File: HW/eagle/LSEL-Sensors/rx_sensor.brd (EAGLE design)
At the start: 22 x 20 mm, 14 parts, among them U1 Tiny45-20-SMT

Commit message: Documents
datasheets, RJ information
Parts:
- JP2: value (none) -> RJ11-2L-B; device SparkFun-Connectors:JST-4-PTH -> con-tycoelectronics:RJ11-NO_SHIELD
- moved JP2 3.75 mm to (25.8, 10.0), turned to 90 degrees
- moved R2 0.25 mm to (15.0, 10.0), flipped to the bottom, turned to 90 degrees
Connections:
- net GND: now also JP2.3; no longer JP2.2
- net SCL: now also JP2.2; no longer JP2.1
- net SDA/MOSI: now also JP2.5; no longer JP2.4
- net VCC: now also JP2.4; no longer JP2.3
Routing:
- net SCL: track 36.6 -> 32.2 mm
- net N$1: track 13.0 -> 9.80 mm
- net SDA/MOSI: track 27.5 -> 25.1 mm
- net VCC: track 11.2 -> 8.99 mm, vias 3 -> 2
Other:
- board size 22 x 20 mm -> 29 x 20 mm
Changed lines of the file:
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@@
 <board>
 <plain>
-<wire x1="0" y1="0" x2="22" y2="0" width="0" layer="20"/>
-<wire x1="22" y1="0" x2="22" y2="20" width="0" layer="20"/>
-<wire x1="22" y1="20" x2="0" y2="20" width="0" layer="20"/>
+<wire x1="0" y1="0" x2="29" y2="0" width="0" layer="20"/>
+<wire x1="29" y1="0" x2="28.75" y2="20" width="0" layer="20"/>
+<wire x1="28.75" y1="20" x2="0" y2="20" width="0" layer="20"/>
 <wire x1="0" y1="20" x2="0" y2="0" width="0" layer="20"/>
 <hole x="2.5" y="17.5" drill="2"/>
@@
 <attribute name="VALUE" x="8.5" y="6.25" size="0.4064" layer="28" font="vector" ratio="15" rot="MR180"/>
 </element>
-<element name="R2" library="SparkFun-Resistors" package="0603-RES" value="1k" x="15" y="10.25" smashed="yes" rot="R270">
-<attribute name="NAME" x="14" y="12" size="0.4064" layer="25" font="vector" ratio="15" rot="R270" align="bottom-right"/>
-<attribute name="VALUE" x="14" y="8.5" size="0.4064" layer="27" font="vector" ratio="15" rot="R270"/>
+<element name="R2" library="SparkFun-Resistors" package="0603-RES" value="1k" x="15" y="10" smashed="yes" rot="MR90">
+<attribute name="NAME" x="14" y="8.25" size="0.4064" layer="26" font="vector" ratio="15" rot="MR90" align="bottom-right"/>
+<attribute name="VALUE" x="14" y="11.75" size="0.4064" layer="28" font="vector" ratio="15" rot="MR90"/>
 </element>
 <element name="R3" library="SparkFun-Resistors" package="0603-RES" value="10k" x="12.5" y="8" smashed="yes" rot="MR270">
@@
 <attribute name="VALUE" x="1" y="7.73" size="0.4064" layer="27" rot="R90"/>
 </element>
-<element name="JP2" library="SparkFun-Connectors" package="JST-4-PTH" value="" x="22" y="10" smashed="yes" rot="R270">
-<attribute name="SKU" value="PRT-09916" x="5.49" y="-9.05" size="1.778" layer="27" rot="R270" display="off"/>
-<attribute name="NAME" x="21.48" y="16.48" size="0.6096" layer="25" font="vector" ratio="15" rot="R90"/>
-<attribute name="VALUE" x="21" y="12.27" size="0.4064" layer="27" rot="R270"/>
+<element name="JP2" library="con-tycoelectronics" package="RJ11-NO_SHIELD" value="RJ11-2L-B" x="25.75" y="10" smashed="yes" rot="R90">
+<attribute name="NAME" x="26.27" y="3.52" size="0.6096" layer="25" font="vector" ratio="15" rot="R270"/>
+<attribute name="VALUE" x="26.75" y="7.73" size="0.4064" layer="27" rot="R90"/>
+<attribute name="OC_FARNELL" value="unknown" x="25.75" y="10" size="1.778" layer="27" rot="R90" display="off"/>
+<attribute name="MF" value="TYCO ELECTRONICS" x="25.75" y="10" size="1.778" layer="27" rot="R90" display="off"/>
+<attribute name="OC_NEWARK" value="83F4463" x="25.75" y="10" size="1.778" layer="27" rot="R90" display="off"/>
+<attribute name="MPN" value="RJ11-2L-B" x="25.75" y="10" size="1.778" layer="27" rot="R90" display="off"/>
 </element>
 <element name="JP3" library="pinhead" package="2X03" value="" x="11" y="2.5" smashed="yes">
@@
 <polygon width="0.4064" layer="1" spacing="0.6096">
 <vertex x="0" y="20"/>
-<vertex x="22" y="20"/>
-<vertex x="22" y="0"/>
+<vertex x="28.5" y="20"/>
+<vertex x="28.5" y="0"/>
 <vertex x="0" y="0"/>
 </polygon>
-<contactref element="JP2" pad="3"/>
+<contactref element="JP2" pad="4"/>
 <contactref element="JP1" pad="2"/>
 <wire x1="9.5" y1="13.15" x2="7.1" y2="13.15" width="0.4064" layer="16"/>
@@
 <wire x1="12.5" y1="7.15" x2="11.85" y2="7.15" width="0.4064" layer="16"/>
 <wire x1="11.85" y1="7.15" x2="10.15" y2="8.85" width="0.4064" layer="16"/>
-<via x="19.25" y="9" extent="1-16" drill="0.3"/>
-<wire x1="19.25" y1="9" x2="17" y2="9" width="1.2" layer="16"/>
 </signal>
 <signal name="GND">
@@
 <polygon width="0.4064" layer="16" spacing="0.6096">
 <vertex x="0" y="0"/>
-<vertex x="22" y="0"/>
-<vertex x="22" y="20"/>
+<vertex x="28.5" y="0"/>
+<vertex x="28.5" y="20"/>
 <vertex x="0" y="20"/>
 </polygon>
 <contactref element="JP1" pad="3"/>
-<contactref element="JP2" pad="2"/>
+<contactref element="JP2" pad="3"/>
 <contactref element="R5" pad="1"/>
 <contactref element="TSOP4836" pad="GND"/>
 <wire x1="5" y1="11" x2="6.85" y2="11" width="0.4064" layer="1"/>
 <wire x1="6.85" y1="11" x2="7" y2="10.85" width="0.4064" layer="1"/>
-<wire x1="17" y1="11" x2="14.9" y2="11" width="0.4064" layer="1"/>
-<wire x1="14.9" y1="11" x2="15" y2="11.1" width="0.4064" layer="1"/>
 <wire x1="15" y1="4.25" x2="14.5" y2="3.75" width="0.4064" layer="1"/>
 <wire x1="14.5" y1="3.75" x2="13.56" y2="3.75" width="0.4064" layer="1"/>
@@
 <wire x1="14.6282" y1="6.6218" x2="15" y2="6.25" width="0.4064" layer="1"/>
 <wire x1="15" y1="6.25" x2="15" y2="4.25" width="0.4064" layer="1"/>
+<wire x1="15" y1="9.15" x2="16.645" y2="9.15" width="0.4064" layer="16"/>
+<wire x1="16.645" y1="9.15" x2="16.86" y2="9.365" width="0.4064" layer="16"/>
 </signal>
 <signal name="N$1">
 <contactref element="LED1" pad="C"/>
 <contactref element="R2" pad="2"/>
-<wire x1="15" y1="9.4" x2="15" y2="8.5" width="0.4064" layer="1"/>
-<via x="15" y="8.5" extent="1-16" drill="0.3"/>
+<wire x1="15" y1="10.85" x2="15" y2="12" width="0.4064" layer="16"/>
+<via x="15" y="12" extent="1-16" drill="0.3"/>
 <via x="17" y="15.5" extent="1-16" drill="0.3"/>
 <wire x1="15.623" y1="19.25" x2="15.623" y2="16.877" width="0.4064" layer="1"/>
 <wire x1="15.623" y1="16.877" x2="17" y2="15.5" width="0.4064" layer="1"/>
-<wire x1="15" y1="8.5" x2="15" y2="12.75" width="0.4064" layer="16"/>
+<wire x1="15" y1="12" x2="15" y2="12.75" width="0.4064" layer="16"/>
 <wire x1="15" y1="12.75" x2="17" y2="14.75" width="0.4064" layer="16"/>
 <wire x1="17" y1="14.75" x2="17" y2="15.5" width="0.4064" layer="16"/>
@@
 <contactref element="U1" pad="7"/>
 <contactref element="JP3" pad="3"/>
-<contactref element="JP2" pad="1"/>
+<contactref element="JP2" pad="2"/>
 <contactref element="JP1" pad="4"/>
 <via x="10.25" y="11.5" extent="1-16" drill="0.3"/>
@@
 <wire x1="11.5" y1="11.5" x2="12.75" y2="10" width="0.4064" layer="16"/>
 <via x="12.75" y="10" extent="1-16" drill="0.3"/>
-<wire x1="12.75" y1="10" x2="14" y2="12.25" width="0.4064" layer="1"/>
+<wire x1="12.75" y1="10" x2="13.75" y2="8" width="0.4064" layer="1"/>
 <wire x1="11" y1="1.23" x2="12.27" y2="2.5" width="0.4064" layer="1"/>
 <wire x1="12.27" y1="2.5" x2="15" y2="2.5" width="0.4064" layer="1"/>
-<wire x1="15" y1="2.5" x2="18.5" y2="5.5" width="0.4064" layer="1"/>
-<wire x1="18.5" y1="5.5" x2="18.5" y2="13" width="0.4064" layer="1"/>
-<wire x1="18.5" y1="13" x2="17" y2="13" width="0.4064" layer="1"/>
 <wire x1="10.365" y1="13.3528" x2="10.365" y2="11.615" width="0.4064" layer="1"/>
 <wire x1="10.365" y1="11.615" x2="10.25" y2="11.5" width="0.4064" layer="1"/>
@@
 <wire x1="9.75" y1="15" x2="7" y2="15" width="0.4064" layer="1"/>
 <wire x1="7" y1="15" x2="5" y2="13" width="0.4064" layer="1"/>
-<wire x1="14" y1="12.25" x2="16.25" y2="12.25" width="0.4064" layer="1"/>
-<wire x1="16.25" y1="12.25" x2="17" y2="13" width="0.4064" layer="1"/>
+<wire x1="13.75" y1="8" x2="18.555" y2="7.75" width="0.4064" layer="1"/>
+<wire x1="18.555" y1="7.75" x2="19.4" y2="8.095" width="0.4064" layer="1"/>
+<wire x1="15" y1="2.5" x2="19" y2="6.5" width="0.4064" layer="1"/>
+<wire x1="19" y1="6.5" x2="19" y2="7.305" width="0.4064" layer="1"/>
+<wire x1="19" y1="7.305" x2="18.555" y2="7.75" width="0.4064" layer="1"/>
 </signal>
 <signal name="RST">
@@
 <contactref element="JP3" pad="4"/>
 <contactref element="JP1" pad="1"/>
-<contactref element="JP2" pad="4"/>
+<contactref element="JP2" pad="5"/>
 <wire x1="12.905" y1="13.3528" x2="12.905" y2="11.405" width="0.4064" layer="1"/>
-<wire x1="12.905" y1="11.405" x2="11.625" y2="10.125" width="0.4064" layer="1"/>
-<wire x1="11.625" y1="10.125" x2="9.75" y2="8.25" width="0.4064" layer="1"/>
+<wire x1="12.905" y1="11.405" x2="9.75" y2="8.25" width="0.4064" layer="1"/>
 <wire x1="9.75" y1="8.25" x2="8.25" y2="8.25" width="0.4064" layer="1"/>
 <wire x1="8.25" y1="8.25" x2="7" y2="7" width="0.4064" layer="1"/>
@@
 <wire x1="7" y1="5" x2="5" y2="7" width="0.4064" layer="16"/>
 <wire x1="12.905" y1="13.3528" x2="13" y2="13.3528" width="0.4064" layer="1"/>
-<wire x1="13" y1="13.3528" x2="13" y2="11.5" width="0.4064" layer="1"/>
-<wire x1="17" y1="7" x2="15.25" y2="7" width="0.4064" layer="1"/>
-<wire x1="15.25" y1="7" x2="11.625" y2="10.125" width="0.4064" layer="1"/>
+<wire x1="13" y1="13.3528" x2="13" y2="12.75" width="0.4064" layer="1"/>
+<wire x1="13" y1="11.5" x2="13" y2="12.75" width="0.4064" layer="1"/>
+<wire x1="13" y1="12.75" x2="15.515" y2="12.75" width="0.4064" layer="1"/>
+<wire x1="15.515" y1="12.75" x2="16.86" y2="11.905" width="0.4064" layer="1"/>
 </signal>
 <signal name="N$3">

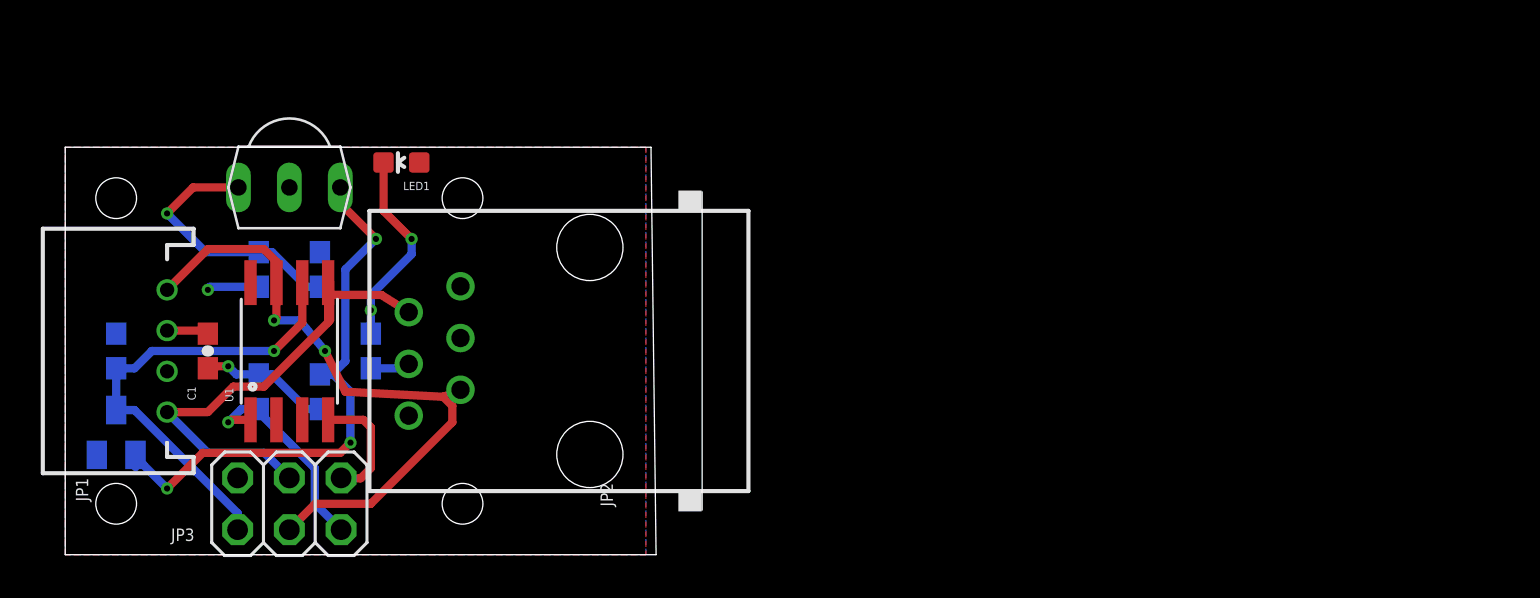
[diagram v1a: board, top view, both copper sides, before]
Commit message: Sensor RJ
Sensor connectors changed
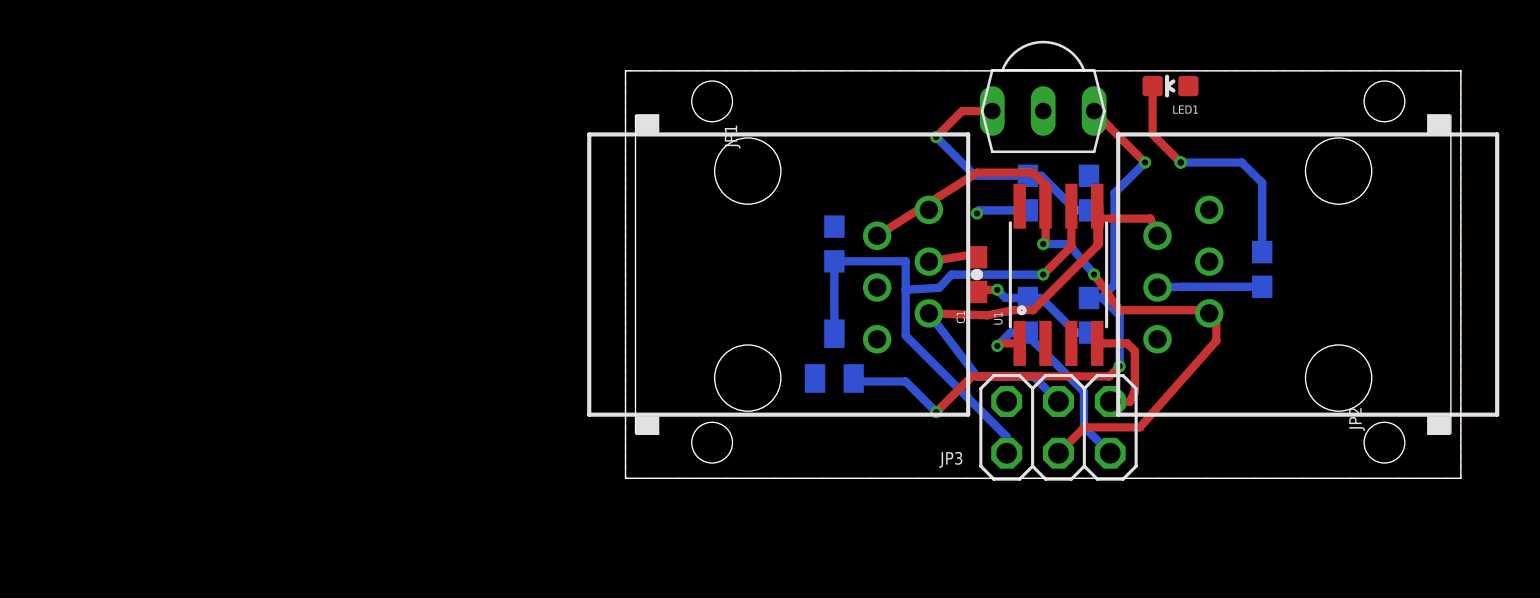
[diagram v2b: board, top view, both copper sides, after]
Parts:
- JP1: value (none) -> RJ11-2L-B; device SparkFun-Connectors:JST-4-PTH -> con-tycoelectronics:RJ11-NO_SHIELD
- moved R2 43.9 mm to (58.8, 14.0)
- moved C1 37.9 mm to (44.8, 13.8)
- moved C2 37.9 mm to (50.2, 17.8)
- moved JP3 37.9 mm to (48.8, 6.25)
- moved LED1 37.9 mm to (54.2, 23.0)
- moved R1 37.9 mm to (47.2, 11.8)
- moved R3 37.9 mm to (50.2, 11.8)
- moved R4 37.9 mm to (47.2, 17.8)
- moved U1 37.9 mm to (48.8, 13.8)
- moved TSOP4836 37.2 mm to (48.0, 21.8)
- moved JP2 36.9 mm to (62.5, 13.8)
- moved R5 35.6 mm to (37.8, 15.2)
- moved D1 35.4 mm to (37.8, 9.75)
- moved JP1 33.7 mm to (33.5, 13.8), turned to 270 degrees
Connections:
- net SCL: now also JP1.2; no longer JP1.4
- net SDA/MOSI: now also JP1.5; no longer JP1.1
- net VCC: now also JP1.4; no longer JP1.2
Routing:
- net MISO: track 22.9 -> 29.5 mm
- net GND: track 9.94 -> 13.1 mm
- net N$1: track 9.80 -> 12.1 mm
- net SCL: track 32.2 -> 34.4 mm
- net SENSOR_OUT: track 28.5 -> 30.7 mm
- net N$2: track 13.0 -> 12.3 mm
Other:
- board size 29 x 20 mm -> 41 x 20 mm

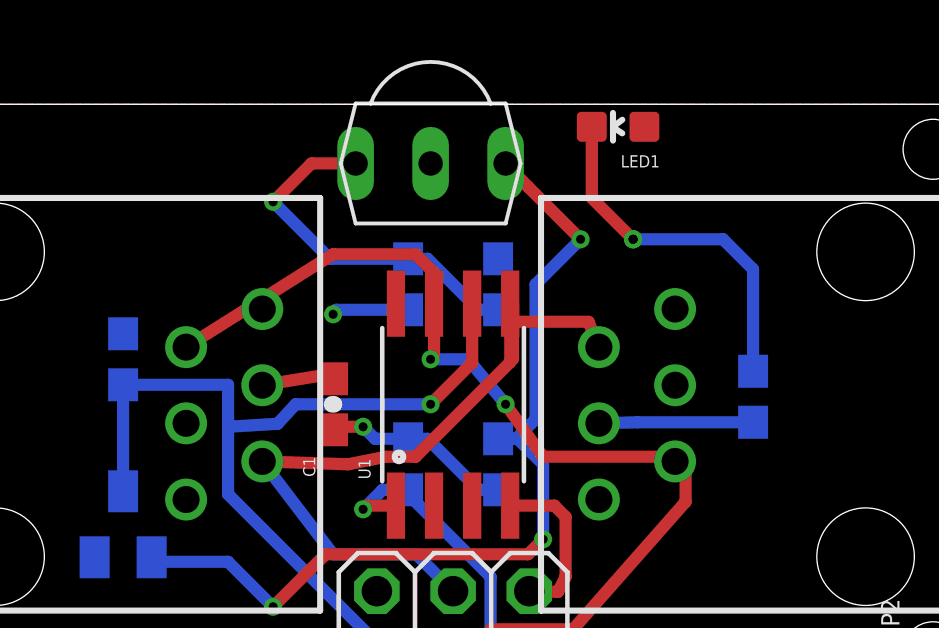
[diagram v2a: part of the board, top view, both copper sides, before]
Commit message: Sensor IR
little changes
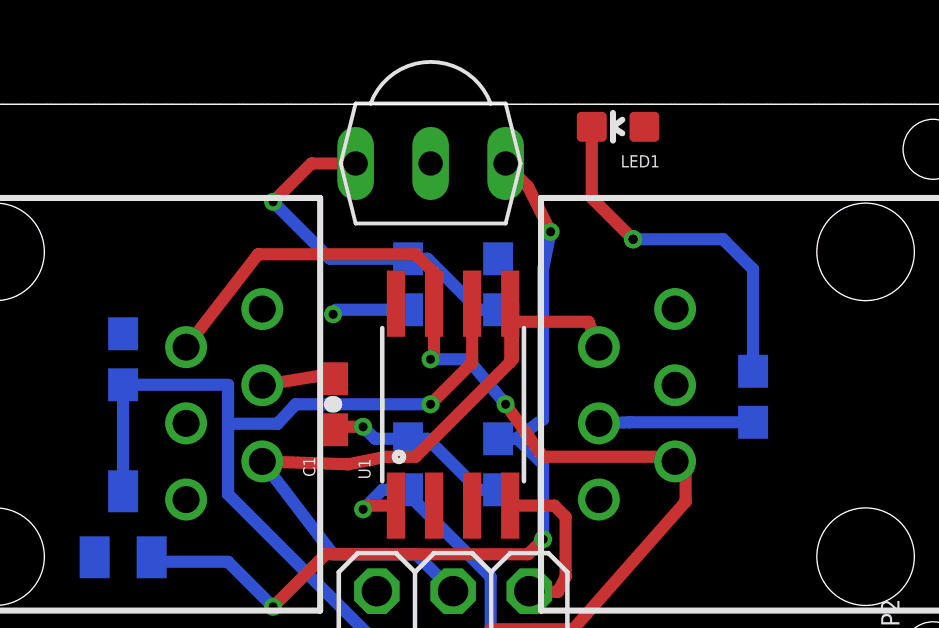
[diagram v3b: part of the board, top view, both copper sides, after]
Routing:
- net SENSOR_OUT: track 30.7 -> 29.2 mm
- net SCL: track 34.4 -> 35.0 mm
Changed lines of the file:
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@@
 <wire x1="52.1282" y1="10.3718" x2="52.5" y2="10" width="0.4064" layer="1"/>
 <wire x1="52.5" y1="10" x2="52.5" y2="8" width="0.4064" layer="1"/>
-<wire x1="58.75" y1="13.15" x2="54.895" y2="13.15" width="0.4064" layer="16"/>
-<wire x1="54.895" y1="13.15" x2="53.61" y2="13.115" width="0.4064" layer="16"/>
+<wire x1="58.75" y1="13.15" x2="54.645" y2="13.15" width="0.4064" layer="16"/>
+<wire x1="54.645" y1="13.15" x2="53.61" y2="13.115" width="0.4064" layer="16"/>
 </signal>
 <signal name="N$1">
@@
 <wire x1="48.115" y1="17.1028" x2="48.115" y2="18.135" width="0.4064" layer="1"/>
 <wire x1="48.115" y1="18.135" x2="47.5" y2="18.75" width="0.4064" layer="1"/>
-<wire x1="47.5" y1="18.75" x2="44.75" y2="18.75" width="0.4064" layer="1"/>
-<wire x1="44.75" y1="18.75" x2="39.85" y2="15.655" width="0.4064" layer="1"/>
+<wire x1="47.5" y1="18.75" x2="42.25" y2="18.75" width="0.4064" layer="1"/>
+<wire x1="42.25" y1="18.75" x2="39.85" y2="15.655" width="0.4064" layer="1"/>
 <wire x1="51.75" y1="12" x2="56.055" y2="12" width="0.4064" layer="1"/>
 <wire x1="56.055" y1="12" x2="56.15" y2="11.845" width="0.4064" layer="1"/>
@@
 <wire x1="46.21" y1="4.98" x2="46.21" y2="5.79" width="0.4064" layer="16"/>
 <wire x1="37.75" y1="14.4" x2="41.25" y2="14.4" width="0.4064" layer="16"/>
-<wire x1="41.25" y1="14.4" x2="41.25" y2="13" width="0.4064" layer="16"/>
-<wire x1="41.25" y1="13" x2="42.9" y2="13.1" width="0.4064" layer="16"/>
 <wire x1="42.9" y1="13.1" x2="43.5" y2="13.75" width="0.4064" layer="16"/>
 <wire x1="43.5" y1="13.75" x2="48" y2="13.75" width="0.4064" layer="16"/>
@@
 <wire x1="49.385" y1="15.135" x2="48" y2="13.75" width="0.4064" layer="1"/>
 <wire x1="41.25" y1="10.75" x2="41.25" y2="13" width="0.4064" layer="16"/>
+<wire x1="41.25" y1="13" x2="41.25" y2="14.4" width="0.4064" layer="16"/>
 <wire x1="46.21" y1="5.79" x2="41.25" y2="10.75" width="0.4064" layer="16"/>
+<wire x1="42.9" y1="13.1" x2="41.35" y2="13.1" width="0.4064" layer="16"/>
+<wire x1="41.35" y1="13.1" x2="41.25" y2="13" width="0.4064" layer="16"/>
 </signal>
 <signal name="SDA/MOSI">
@@
 <wire x1="51.25" y1="8.75" x2="51.75" y2="9.25" width="0.4064" layer="1"/>
 <via x="51.75" y="9.25" extent="1-16" drill="0.3"/>
-<wire x1="51.5" y1="13.25" x2="51.5" y2="17.75" width="0.4064" layer="16"/>
-<wire x1="51.5" y1="17.75" x2="53" y2="19.25" width="0.4064" layer="16"/>
-<via x="53" y="19.25" extent="1-16" drill="0.3"/>
-<wire x1="53" y1="19.25" x2="51.2512" y2="20.9988" width="0.4064" layer="1"/>
+<wire x1="51.75" y1="13.25" x2="51.75" y2="18.25" width="0.4064" layer="16"/>
+<wire x1="51.75" y1="18.25" x2="52" y2="19.5" width="0.4064" layer="16"/>
+<via x="52" y="19.5" extent="1-16" drill="0.3"/>
+<wire x1="52" y1="19.5" x2="51.2512" y2="20.9988" width="0.4064" layer="1"/>
 <wire x1="51.2512" y1="20.9988" x2="50.5012" y2="21.7766" width="0.4064" layer="1"/>
 <wire x1="51.75" y1="9.25" x2="51.75" y2="11.75" width="0.4064" layer="16"/>
 <wire x1="51.75" y1="11.75" x2="50.9" y2="12.6" width="0.4064" layer="16"/>
-<wire x1="50.25" y1="12.6" x2="50.9" y2="12.6" width="0.4064" layer="16"/>
+<wire x1="50.85" y1="12.6" x2="50.9" y2="12.6" width="0.4064" layer="16"/>
 <wire x1="50.25" y1="12.6" x2="50.85" y2="12.6" width="0.4064" layer="16"/>
-<wire x1="50.85" y1="12.6" x2="51.5" y2="13.25" width="0.4064" layer="16"/>
+<wire x1="50.85" y1="12.6" x2="51.75" y2="13.25" width="0.4064" layer="16"/>
 <wire x1="42.75" y1="7" x2="41.25" y2="8.5" width="0.4064" layer="16"/>
 <wire x1="41.25" y1="8.5" x2="38.85" y2="8.5" width="0.4064" layer="16"/>
